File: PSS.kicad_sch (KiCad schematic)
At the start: 26 parts, among them U2 0.1XS, U3 0.1XS, U4 TSR1-2450E, U5 ADP124, U6 ADP124

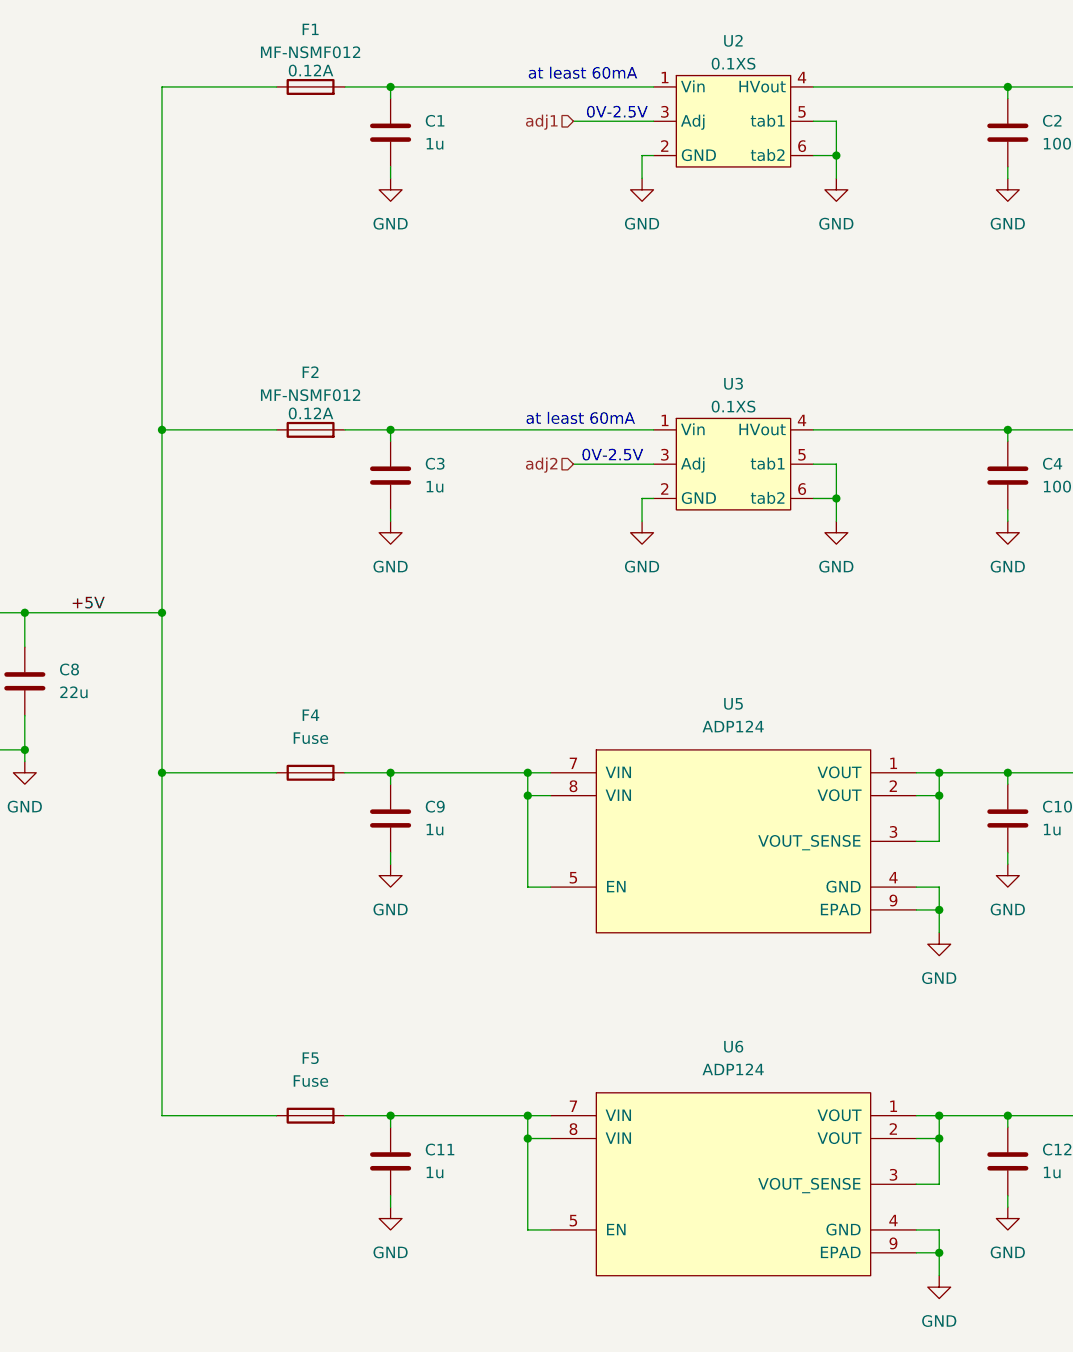
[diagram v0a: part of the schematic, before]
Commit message: adj divider signal
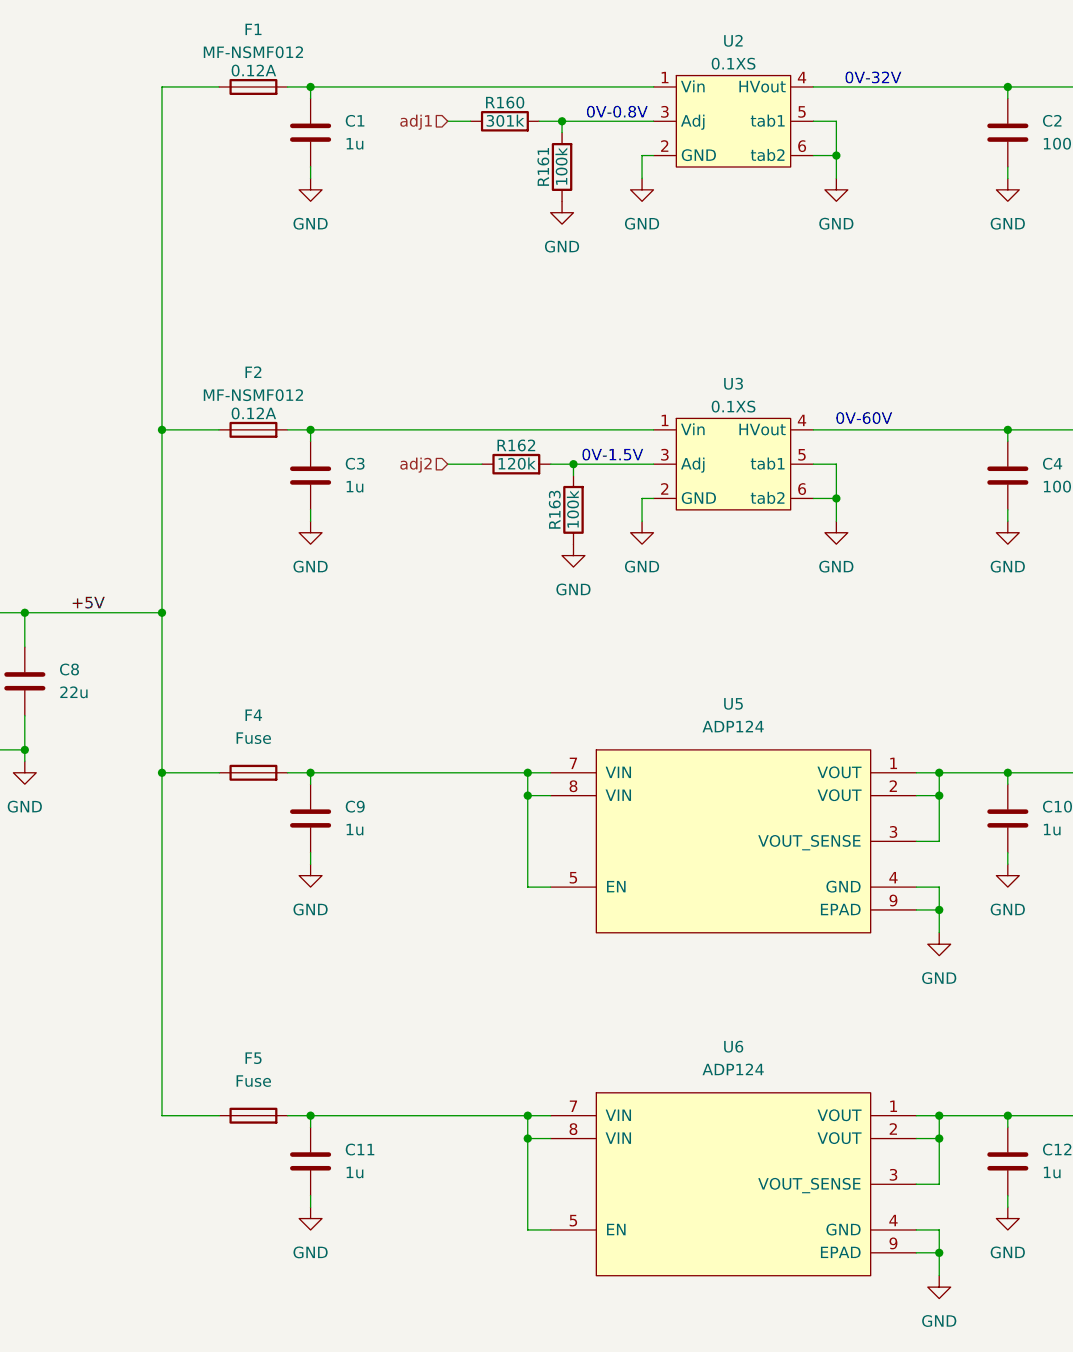
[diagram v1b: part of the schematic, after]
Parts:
- added R160: 301k, Resistor_SMD:R_0603_1608Metric_Pad0.98x0.95mm_HandSolder, symbol Device:R
- added R161, R163: 100k, Resistor_SMD:R_0603_1608Metric_Pad0.98x0.95mm_HandSolder, symbol Device:R
- added R162: 120k, Resistor_SMD:R_0603_1608Metric_Pad0.98x0.95mm_HandSolder, symbol Device:R
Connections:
- net GND: now also R161.1, R163.1
- net adj1: now also R160.1; no longer U2.3 (Adj)
- net adj2: now also R162.1; no longer U3.3 (Adj)
- new net: R162.2, R163.2, U3.3 (Adj)
- new net: R160.2, R161.2, U2.3 (Adj)
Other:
- note added: "0V-0.8V"
- note added: "0V-1.5V"
- note added: "0V-32V"
- note added: "0V-60V"
- note removed: "0V-2.5V"
- note removed: "at least 60mA"
- moved on the sheet: C1, C11, C3, C9, F1, F2, F4, F5

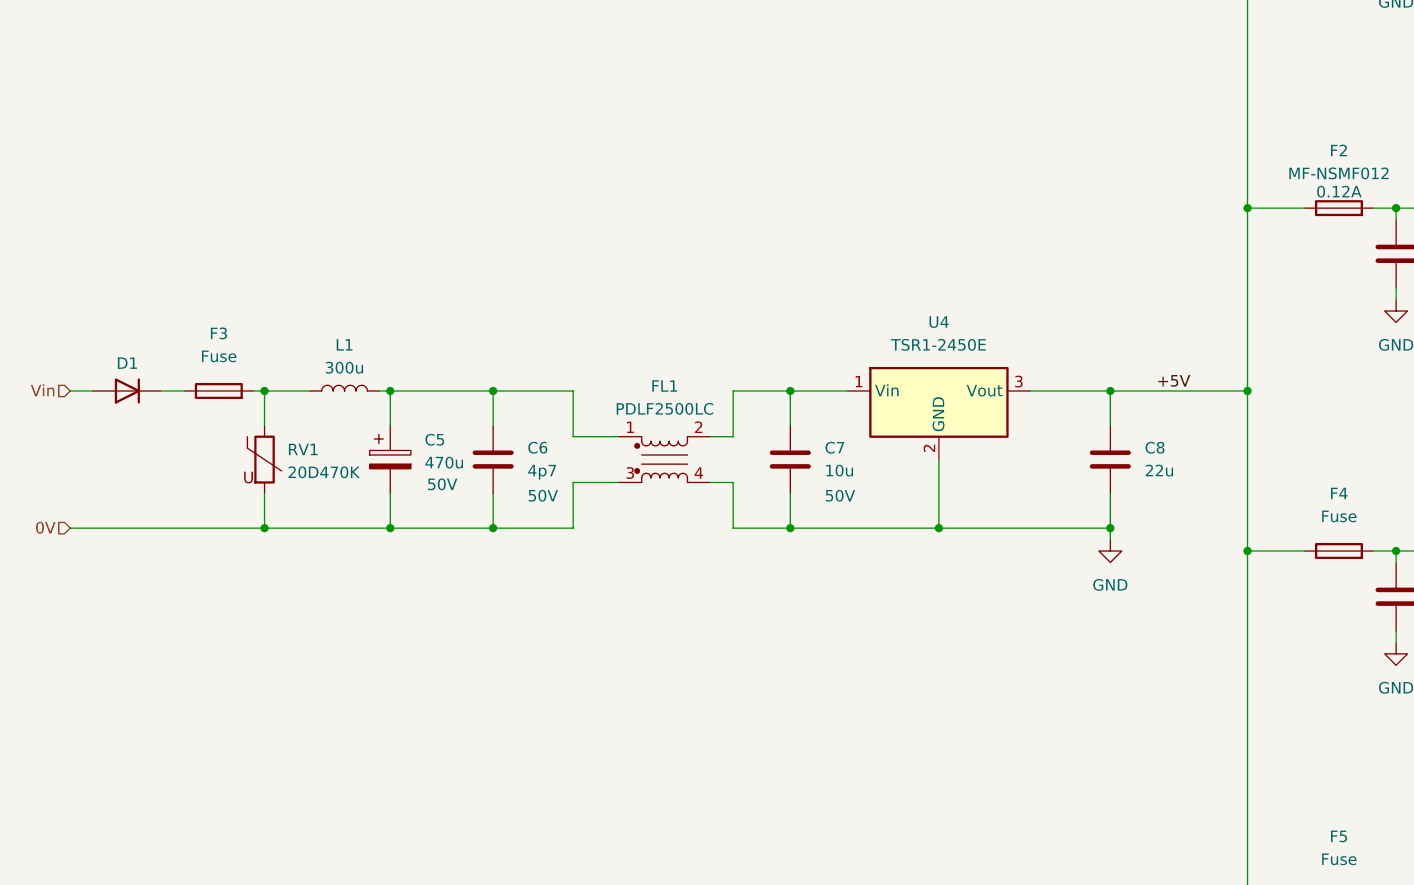
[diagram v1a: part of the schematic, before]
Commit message: 5V dcdc redundancy
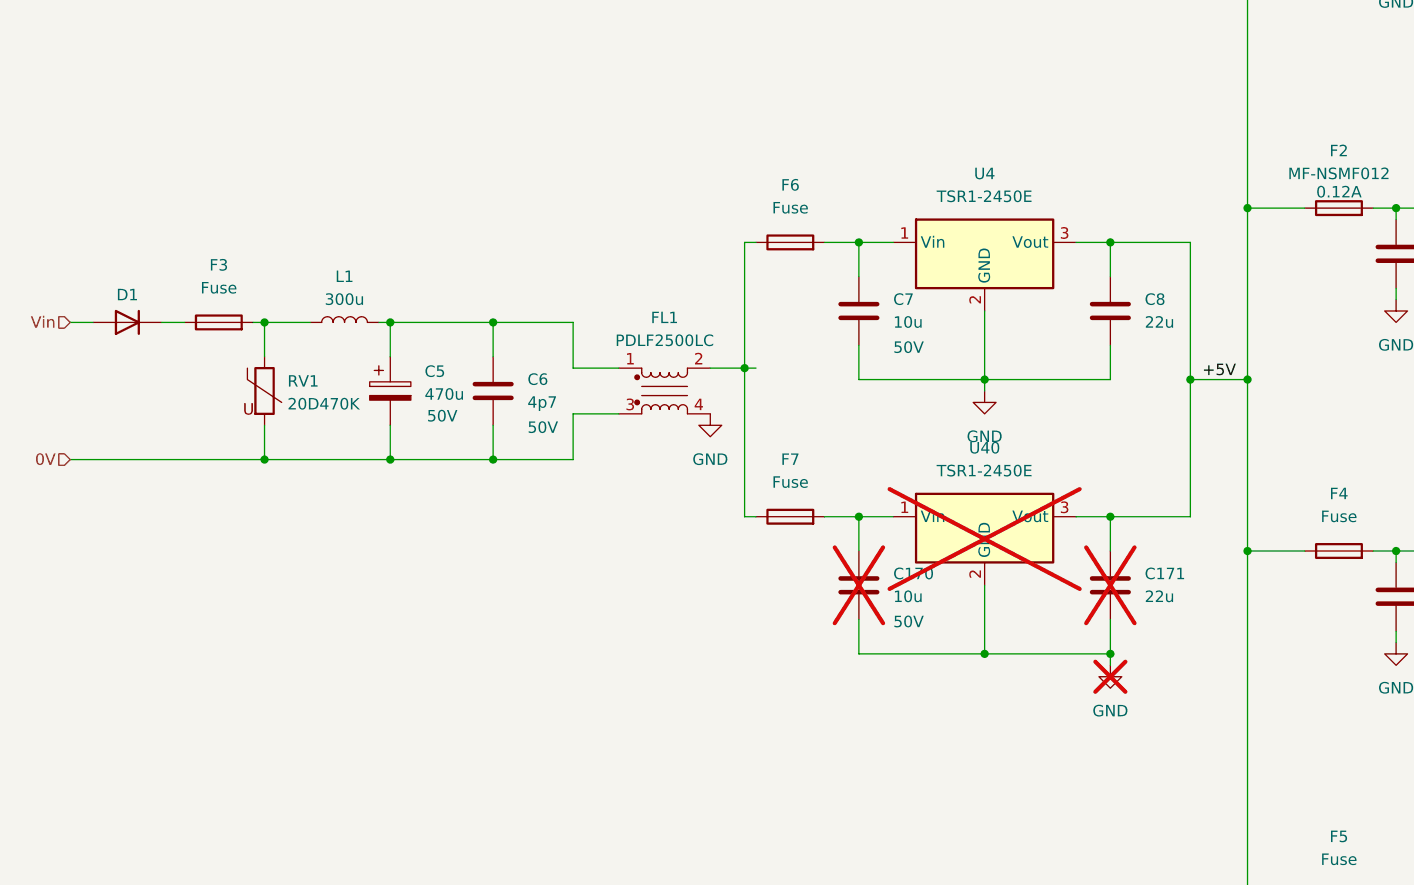
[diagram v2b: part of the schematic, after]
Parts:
- added C170: 10u, symbol Device:C
- added C171: 22u, symbol Device:C
- added F6, F7: Fuse, symbol Device:Fuse
- added U40: TSR1-2450E, Converter_DCDC:Converter_DCDC_TRACO_TSR1-xxxxE_THT, symbol Regulator_Switching:TSR1-2450E
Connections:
- net +5V: now also C171.1, U40.3 (Vout)
- net GND: now also C170.2, C171.2, U40.2 (GND)
- net at C7.1, U4.1 (Vin): now also F6.2; no longer FL1.2
- new net: C170.1, F7.2, U40.1 (Vin)
- new net: F6.1, F7.1, FL1.2
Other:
- moved on the sheet: C5, C6, C7, C8, D1, F3, FL1, L1, RV1, U4

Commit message: data ready signals
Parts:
- added D8, D9: D, symbol Device:D
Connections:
- net +5V: now also D8.1 (K), D9.1 (K); no longer C171.1, C8.1, U4.3 (Vout), U40.3 (Vout)
- new net: C8.1, D8.2 (A), U4.3 (Vout)
- new net: C171.1, D9.2 (A), U40.3 (Vout)
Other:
- moved on the sheet: C7, C8, F6, U4

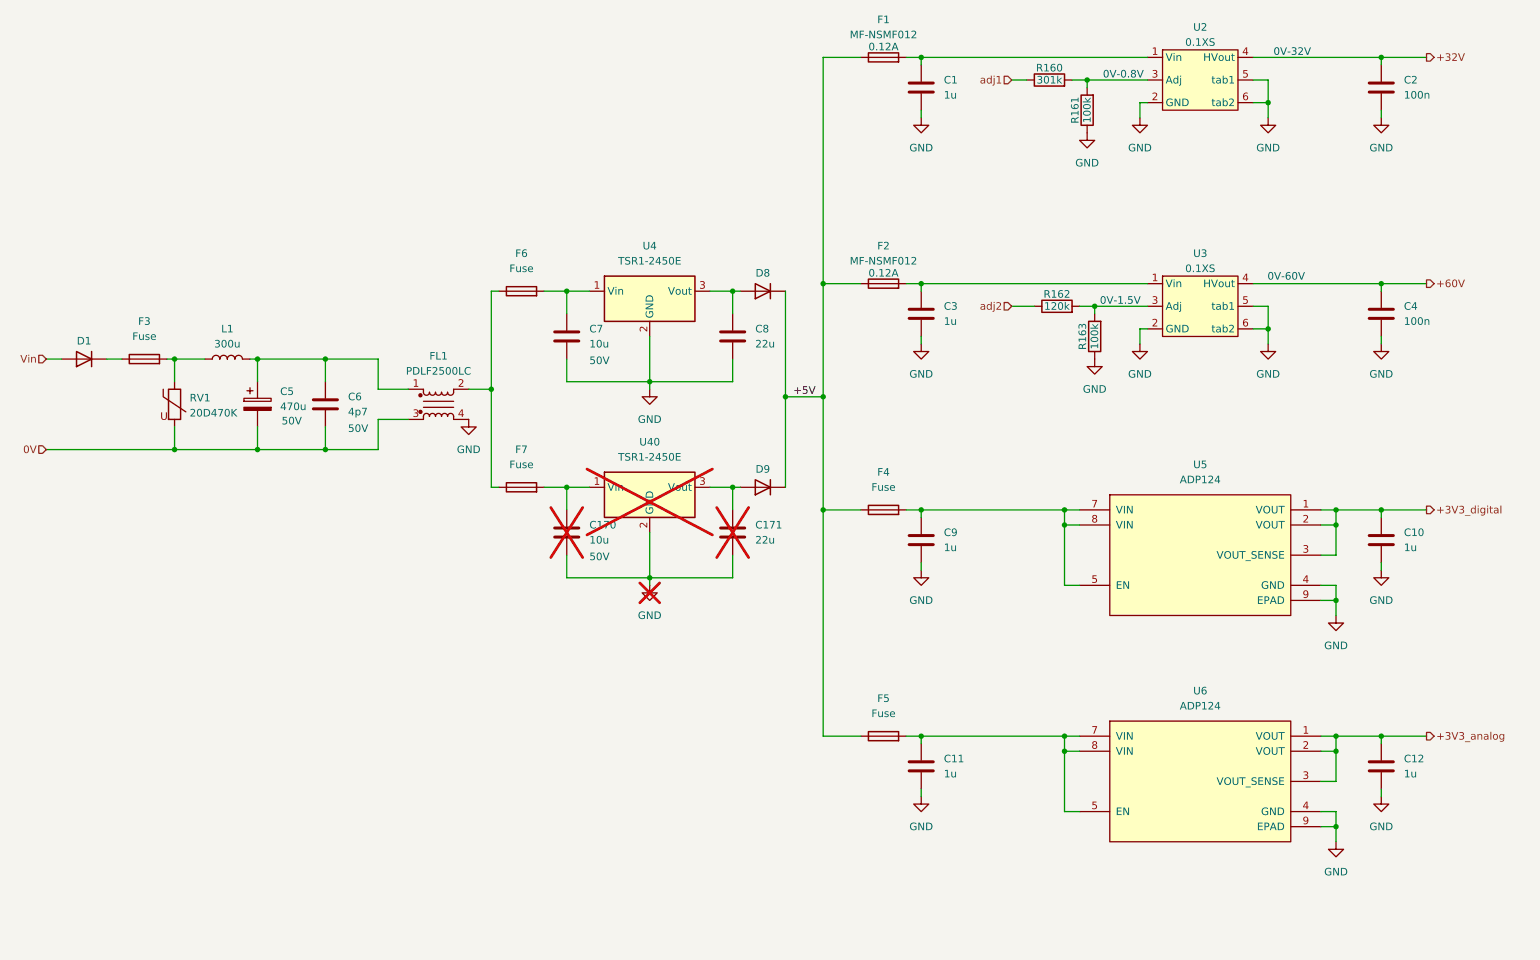
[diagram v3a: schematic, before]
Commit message: gnd and gnda
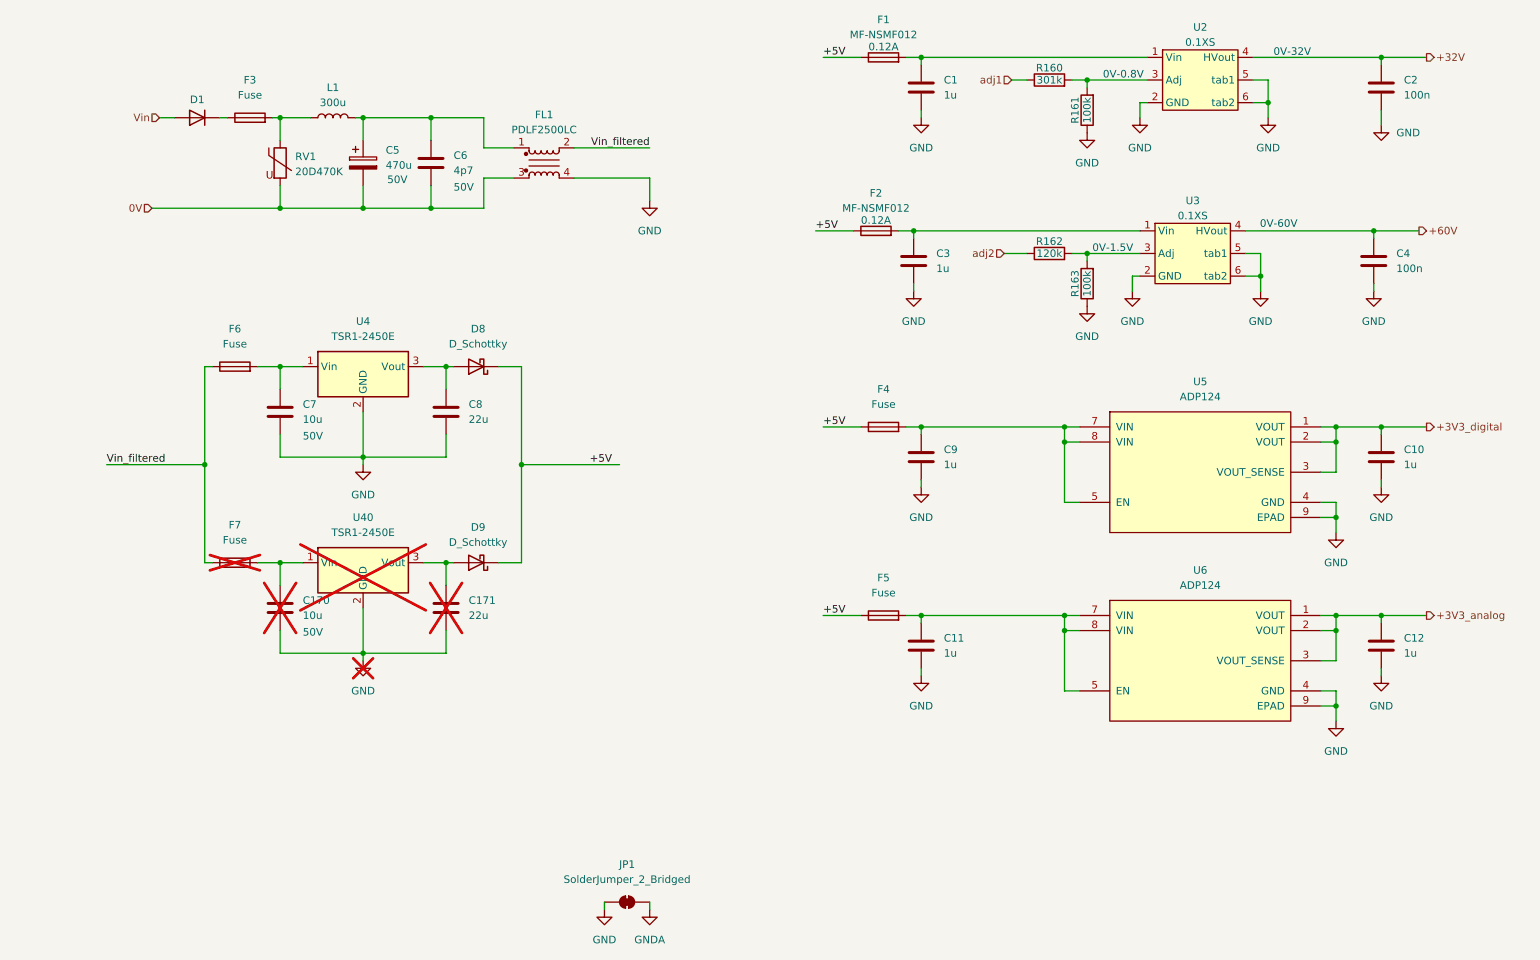
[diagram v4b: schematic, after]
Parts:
- removed D8, D9: D, symbol Device:D
- added D8, D9: D_Schottky, symbol Device:D_Schottky
- added JP1: SolderJumper_2_Bridged, Jumper:SolderJumper-2_P1.3mm_Bridged2Bar_Pad1.0x1.5mm, symbol Jumper:SolderJumper_2_Bridged
- F7: now not fitted
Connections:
- net +5V: now also D8.1 (K), D9.1 (K)
- net GND: now also JP1.1 (A)
- net at C8.1, U4.3 (Vout): now also D8.2 (A)
- net at C171.1, U40.3 (Vout): now also D9.2 (A)
- net Vin_filtered: now reaches F6.1, F7.1, FL1.2
- new net GNDA: JP1.2 (B)
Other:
- moved on the sheet: C10, C11, C12, C3, C4, C9, F2, F4, F5, R162, R163, U3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
